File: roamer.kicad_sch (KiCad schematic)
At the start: 0 parts

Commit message: Added MCU power circuitry. Added LoRa module. Added BME680 circuitry.
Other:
- added sheet Comms - LoRa (comms-lora.kicad_sch)
- added sheet Interface - uUSB (interface-uusb.kicad_sch)
- added sheet MCU (mcu.kicad_sch)
- added sheet MCU - Memory (mcu-memory.kicad_sch)
- added sheet MCU - Oscillator (mcu-oscillator.kicad_sch)
- added sheet Neopixel (neopixel.kicad_sch)
- added sheet Power - Battery (power-battery.kicad_sch)
- added sheet Power - Management (power-management.kicad_sch)
- added sheet Reset Button (reset-button.kicad_sch)
- added sheet Sensor - Air Quality (sensor-air.kicad_sch)
- added sheet Sensor - Atmosphere (sensor-atmosphere.kicad_sch)
- added sheet Sensor - Current (sensor-current.kicad_sch)
- company: blame- steven.clark@stanford.edu -> catbranchman
- title: Test sheet -> Roamer Environmental Sensing

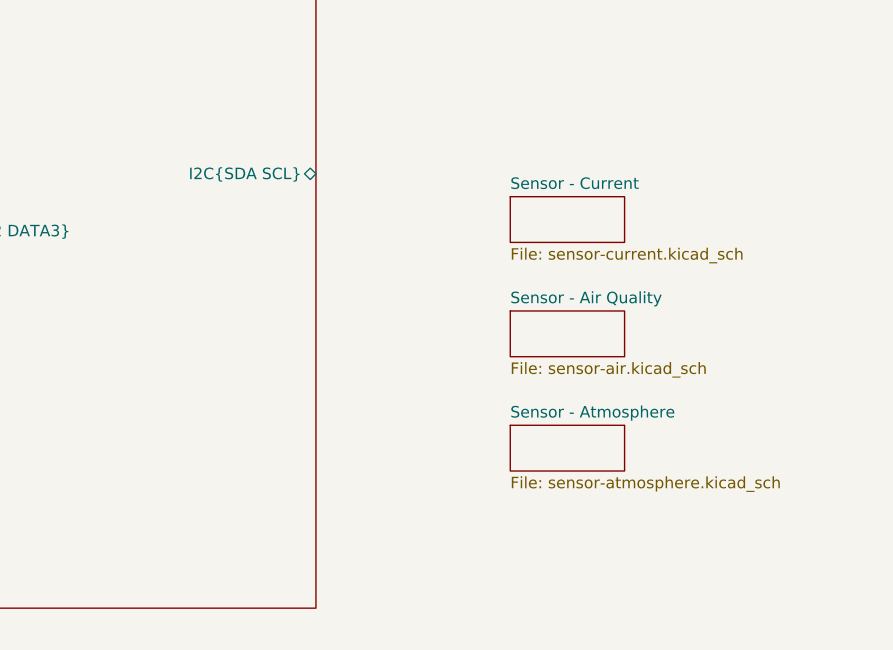
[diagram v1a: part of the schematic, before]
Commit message: Adding I2C bus to circuit
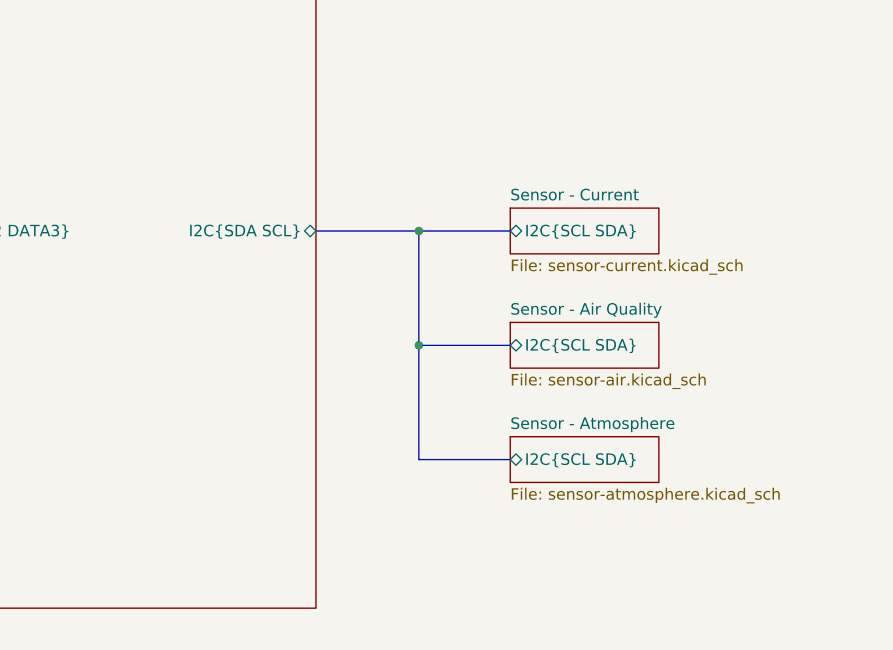
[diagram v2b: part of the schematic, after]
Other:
- sheet Sensor - Air Quality ports: added I2C{SCL SDA}; removed none
- sheet Sensor - Atmosphere ports: added I2C{SCL SDA}; removed none
- sheet Sensor - Current ports: added I2C{SCL SDA}; removed none
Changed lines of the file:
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@@
 		(comment 4 "EE 156 / Stanford University")
+	)
+	(junction
+		(at 293.37 105.41)
+		(diameter 0)
+		(color 0 0 0 0)
+	)
+	(junction
+		(at 293.37 92.71)
+		(diameter 0)
+		(color 0 0 0 0)
 	)
 	(wire
@@
 		)
 	)
+	(bus
+		(pts
+			(xy 293.37 118.11) (xy 293.37 105.41)
+		)
+		(stroke
+			(width 0)
+			(type default)
+		)
+	)
+	(bus
+		(pts
+			(xy 303.53 105.41) (xy 293.37 105.41)
+		)
+		(stroke
+			(width 0)
+			(type default)
+		)
+	)
 	(wire
 		(pts
@@
 		)
 	)
+	(bus
+		(pts
+			(xy 303.53 118.11) (xy 293.37 118.11)
+		)
+		(stroke
+			(width 0)
+			(type default)
+		)
+	)
 	(wire
 		(pts
@@
 		(pts
 			(xy 189.23 78.74) (xy 214.63 78.74)
+		)
+		(stroke
+			(width 0)
+			(type default)
+		)
+	)
+	(bus
+		(pts
+			(xy 293.37 92.71) (xy 281.94 92.71)
+		)
+		(stroke
+			(width 0)
+			(type default)
+		)
+	)
+	(bus
+		(pts
+			(xy 303.53 92.71) (xy 293.37 92.71)
+		)
+		(stroke
+			(width 0)
+			(type default)
+		)
+	)
+	(bus
+		(pts
+			(xy 293.37 105.41) (xy 293.37 92.71)
 		)
 		(stroke
@@
 	)
 	(sheet
-		(at 303.53 114.3)
-		(size 12.7 5.08)
+		(at 303.53 115.57)
+		(size 16.51 5.08)
 		(fields_autoplaced yes)
 		(stroke
@@
 		)
 		(property "Sheetname" "Sensor - Atmosphere"
-			(at 303.53 113.5884 0)
+			(at 303.53 114.8584 0)
 			(effects
 				(font
@@
 		)
 		(property "Sheetfile" "sensor-atmosphere.kicad_sch"
-			(at 303.53 119.9646 0)
+			(at 303.53 121.2346 0)
 			(effects
 				(font
@@
 				)
 				(justify left top)
+			)
+		)
+		(pin "I2C{SCL SDA}" bidirectional
+			(at 303.53 118.11 180)
+			(effects
+				(font
+					(size 1.27 1.27)
+				)
+				(justify left)
 			)
 		)
@@
 	)
 	(sheet
-		(at 303.53 101.6)
-		(size 12.7 5.08)
+		(at 303.53 102.87)
+		(size 16.51 5.08)
 		(fields_autoplaced yes)
 		(stroke
@@
 		)
 		(property "Sheetname" "Sensor - Air Quality"
-			(at 303.53 100.8884 0)
+			(at 303.53 102.1584 0)
 			(effects
 				(font
@@
 		)
 		(property "Sheetfile" "sensor-air.kicad_sch"
-			(at 303.53 107.2646 0)
+			(at 303.53 108.5346 0)
 			(effects
 				(font
@@
 				)
 				(justify left top)
+			)
+		)
+		(pin "I2C{SCL SDA}" bidirectional
+			(at 303.53 105.41 180)
+			(effects
+				(font
+					(size 1.27 1.27)
+				)
+				(justify left)
 			)
 		)
@@
 	)
 	(sheet
-		(at 303.53 88.9)
-		(size 12.7 5.08)
+		(at 303.53 90.17)
+		(size 16.51 5.08)
 		(fields_autoplaced yes)
 		(stroke
@@
 		)
 		(property "Sheetname" "Sensor - Current"
-			(at 303.53 88.1884 0)
+			(at 303.53 89.4584 0)
 			(effects
 				(font
@@
 		)
 		(property "Sheetfile" "sensor-current.kicad_sch"
-			(at 303.53 94.5646 0)
+			(at 303.53 95.8346 0)
 			(effects
 				(font
@@
 				)
 				(justify left top)
+			)
+		)
+		(pin "I2C{SCL SDA}" bidirectional
+			(at 303.53 92.71 180)
+			(effects
+				(font
+					(size 1.27 1.27)
+				)
+				(justify left)
 			)
 		)
@@
 		)
 		(pin "I2C{SDA SCL}" bidirectional
-			(at 281.94 86.36 0)
-			(effects
-				(font
+			(at 281.94 92.71 0)
+			(effects
+				(font

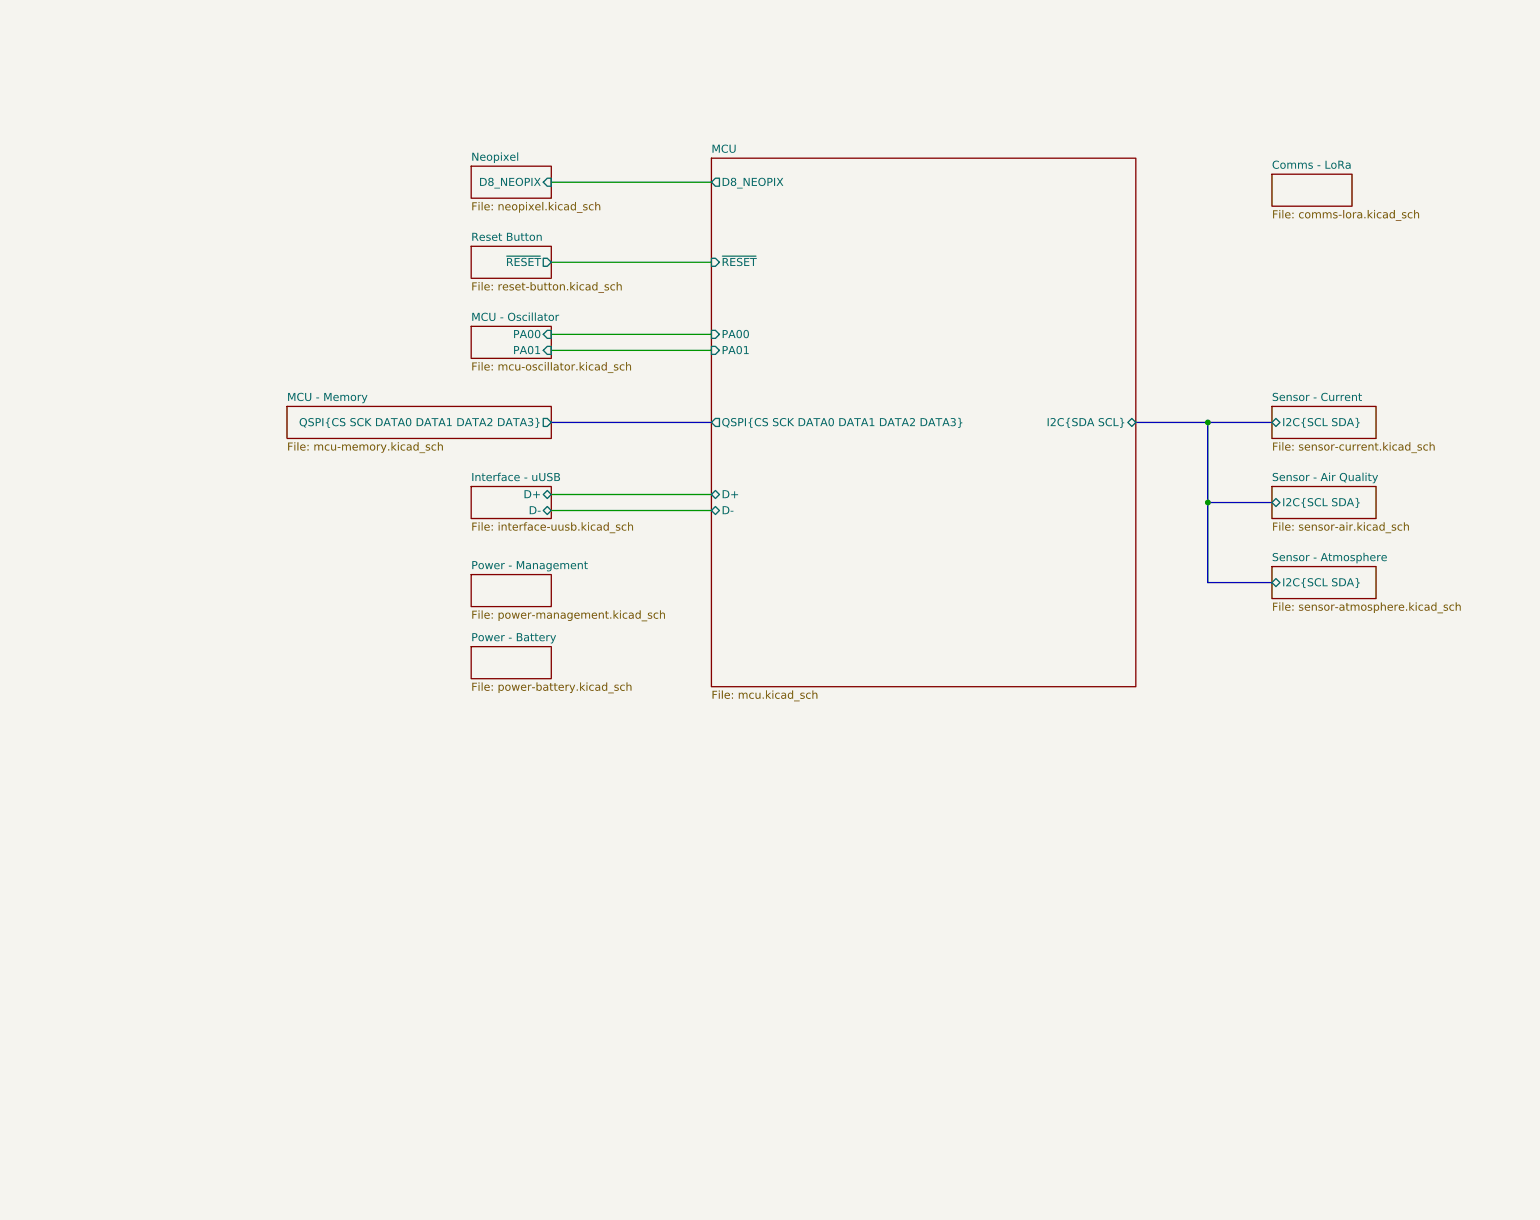
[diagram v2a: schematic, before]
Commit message: Adding symbols information
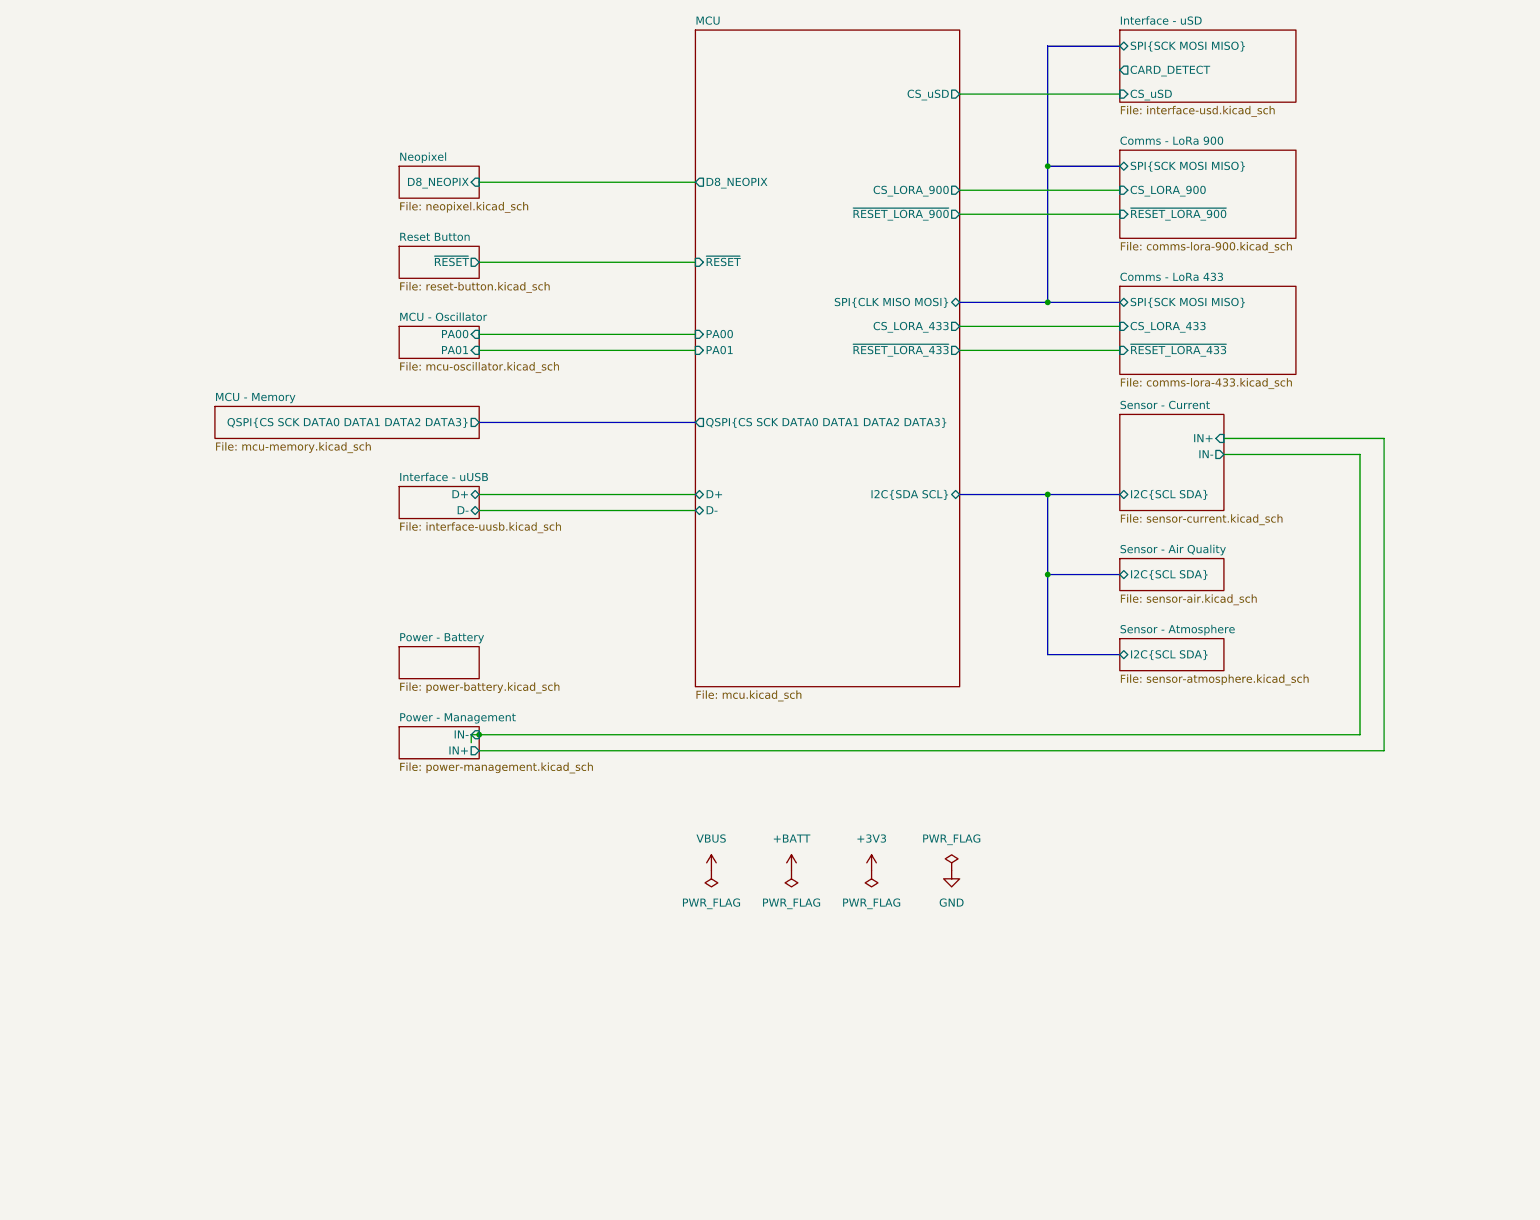
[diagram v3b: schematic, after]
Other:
- sheet Comms - LoRa renamed Comms - LoRa 900
- added sheet Comms - LoRa 433 (comms-lora-433.kicad_sch)
- added sheet Interface - uSD (interface-usd.kicad_sch)
- sheet Comms - LoRa 900: file comms-lora.kicad_sch -> comms-lora-900.kicad_sch
- sheet Comms - LoRa 900 ports: added CS_LORA_900, SPI{SCK MOSI MISO}, ~{RESET_LORA_900}; removed none
- sheet MCU ports: added CS_LORA_433, CS_LORA_900, CS_uSD, SPI{CLK MISO MOSI}, ~{RESET_LORA_433}, ~{RESET_LORA_900}; removed none
- sheet Power - Management ports: added IN+, IN-; removed none
- sheet Sensor - Current ports: added IN+, IN-; removed none

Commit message: Adding rest of schematic
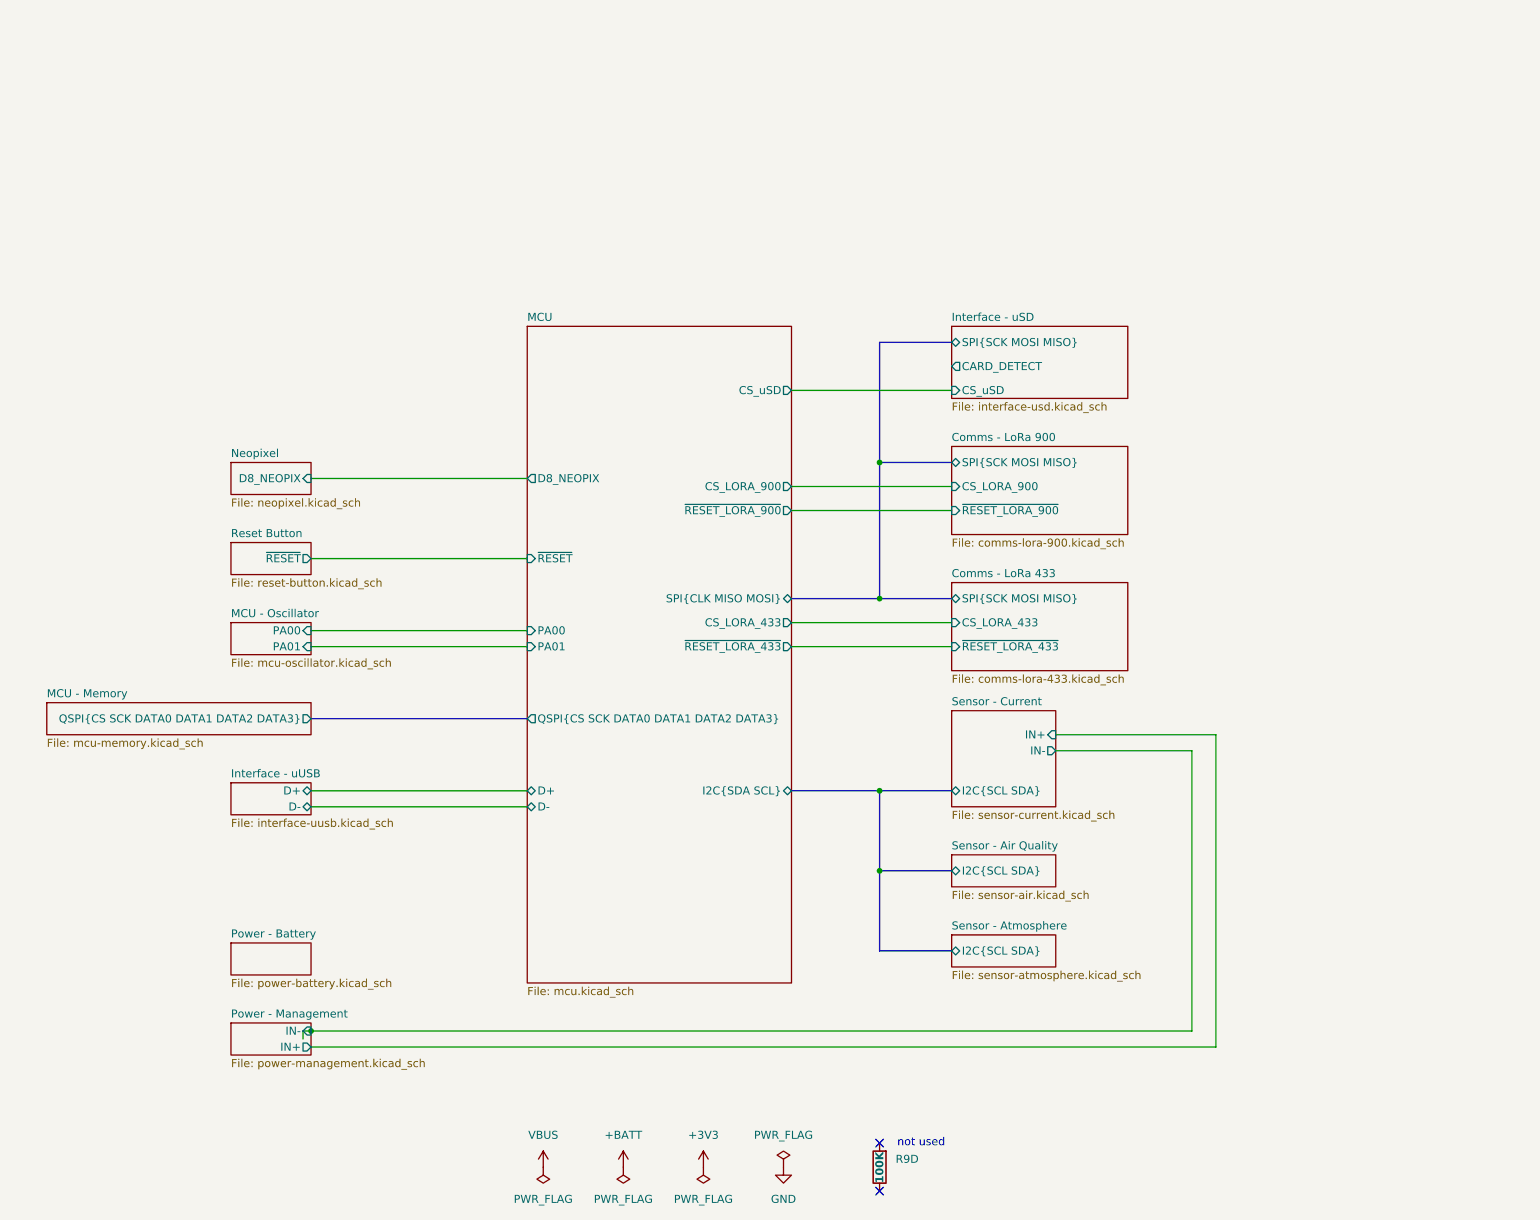
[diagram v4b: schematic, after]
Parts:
- added R9D: 100K, Resistor_SMD:R_Array_Convex_4x1206, symbol Device:R
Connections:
- no-connect marks 0 -> 2
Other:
- note added: "not used"

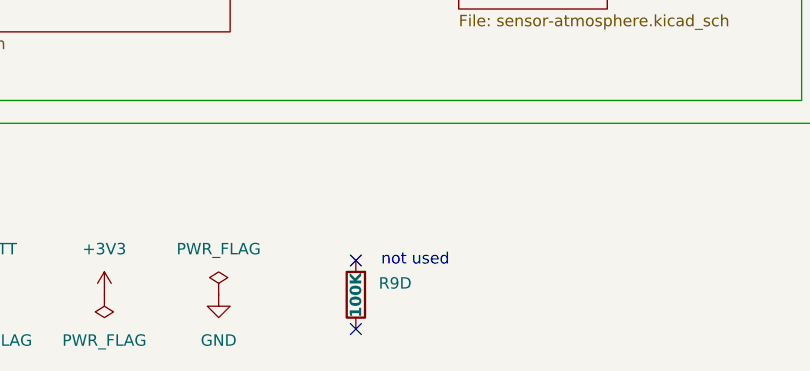
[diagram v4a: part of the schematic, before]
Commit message: Fixing footprint imports
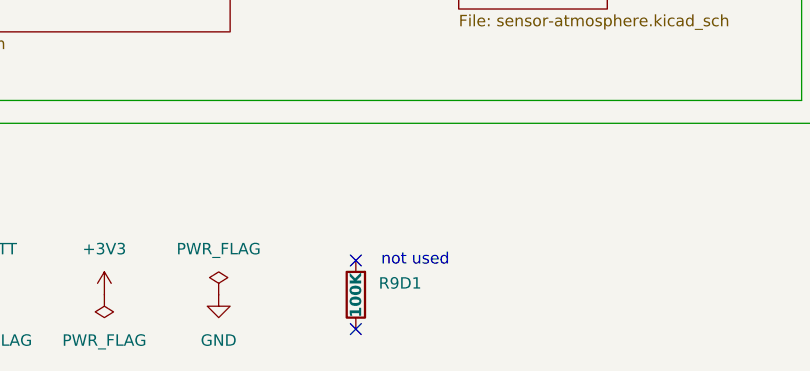
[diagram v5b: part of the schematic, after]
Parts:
- renumbered R9D to R9D1
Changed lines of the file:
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@@
 		(on_board yes)
 		(dnp no)
-		(property "Reference" "R9D"
+		(property "Reference" "R9D1"
 			(at 243.84 209.5499 0)
 			(effects
@@
 			(project "roamer"
 				(path "/1c59de6a-87fe-4223-8898-4b0383164a31"
-					(reference "R9D")
+					(reference "R9D1")
 					(unit 1)
 				)
